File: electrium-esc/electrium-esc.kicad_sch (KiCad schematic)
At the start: 0 parts

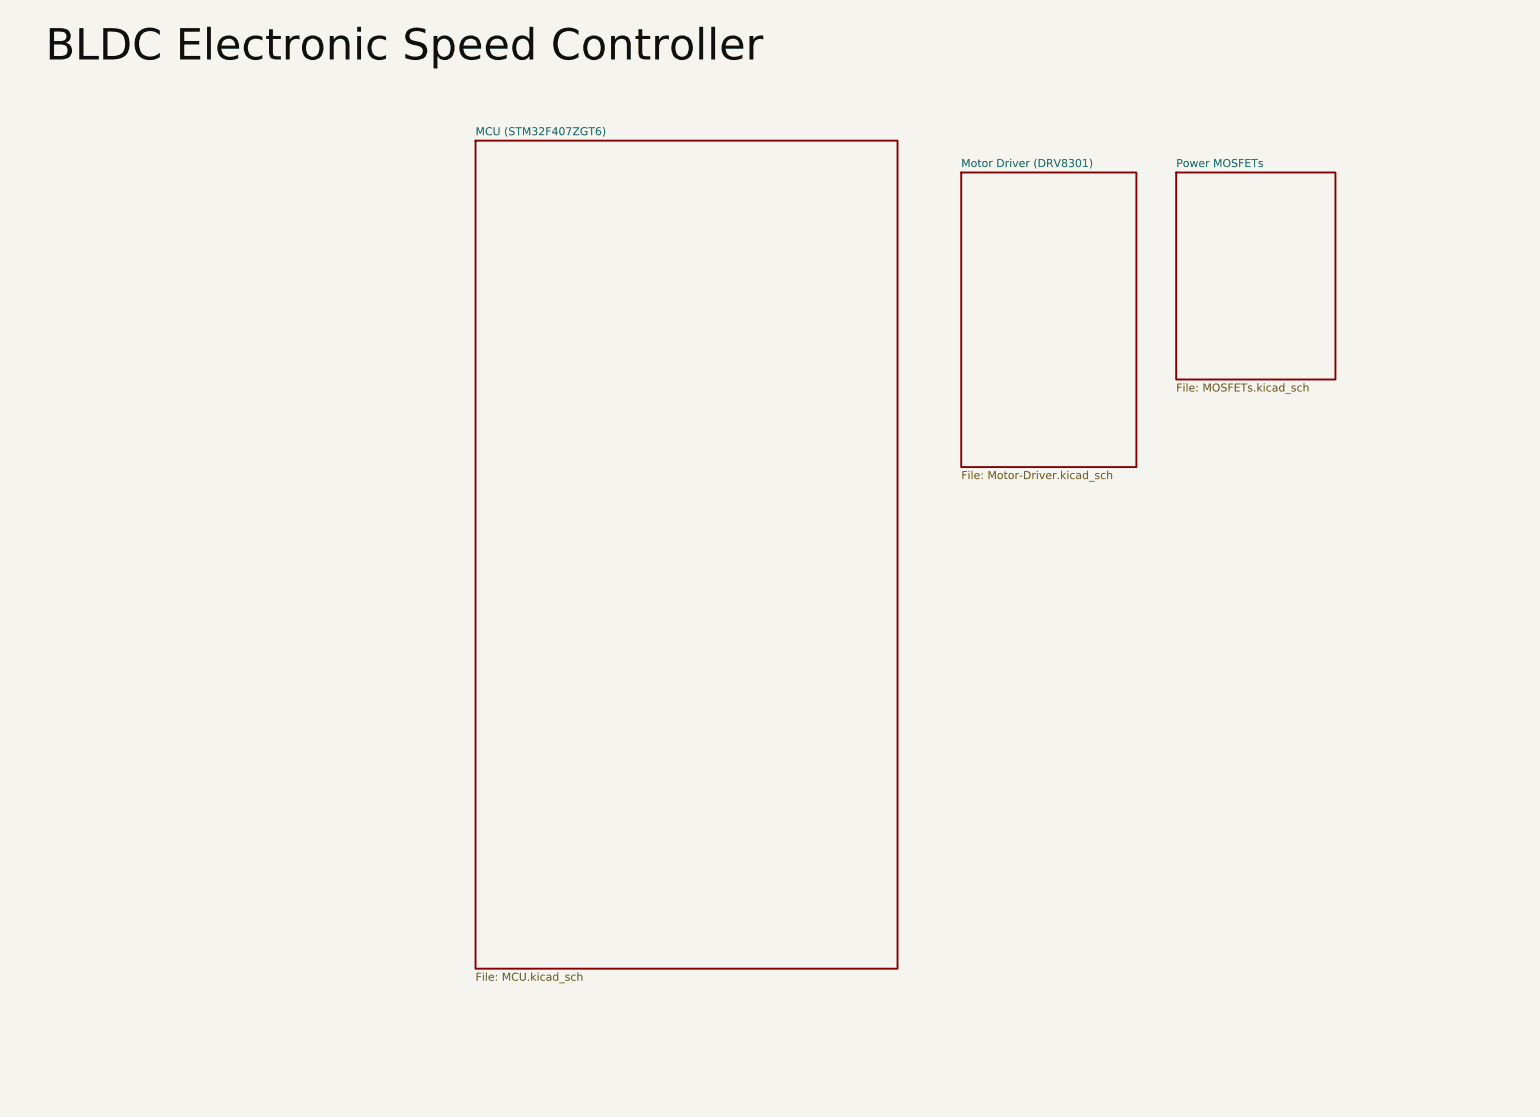
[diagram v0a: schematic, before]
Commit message: Complete Motor Driver!
Put in place passive components per documentation
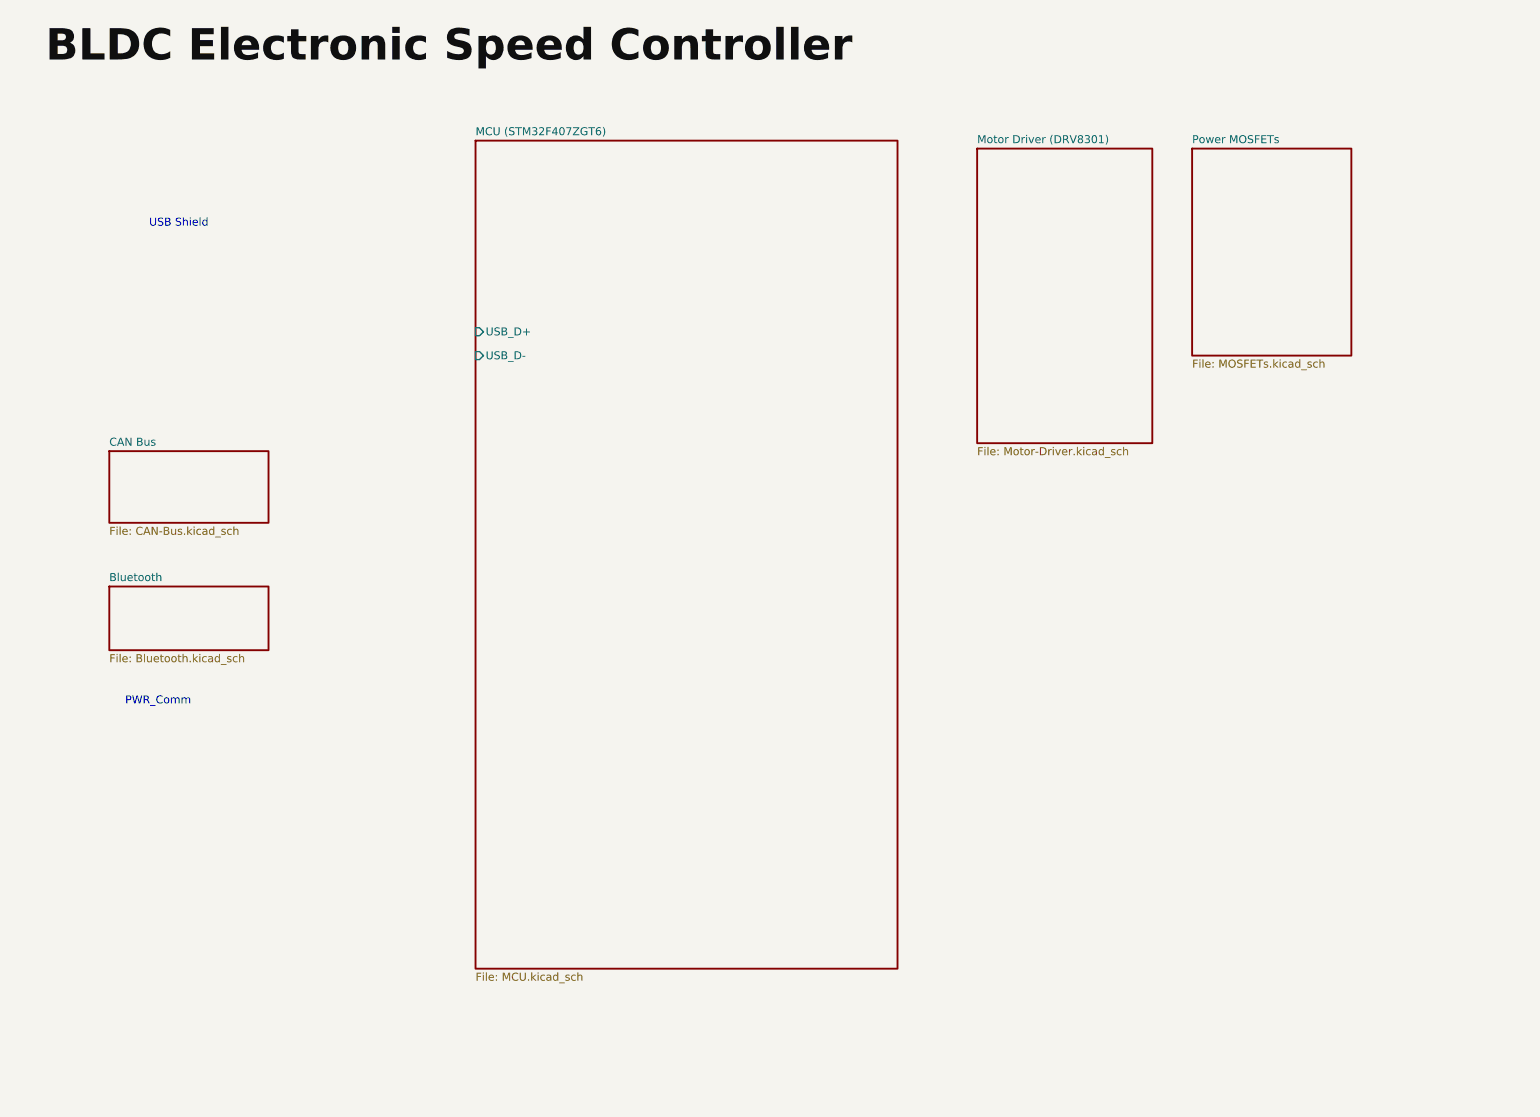
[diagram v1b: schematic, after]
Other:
- added sheet Bluetooth (Bluetooth.kicad_sch)
- added sheet CAN Bus (CAN-Bus.kicad_sch)
- sheet MCU (STM32F407ZGT6) ports: added USB_D+, USB_D-; removed none
- note added: "PWR_Comm"
- note added: "USB Shield"

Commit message: Add additional MCU connectivity
Still need to integrate NRF24L01 capabilities
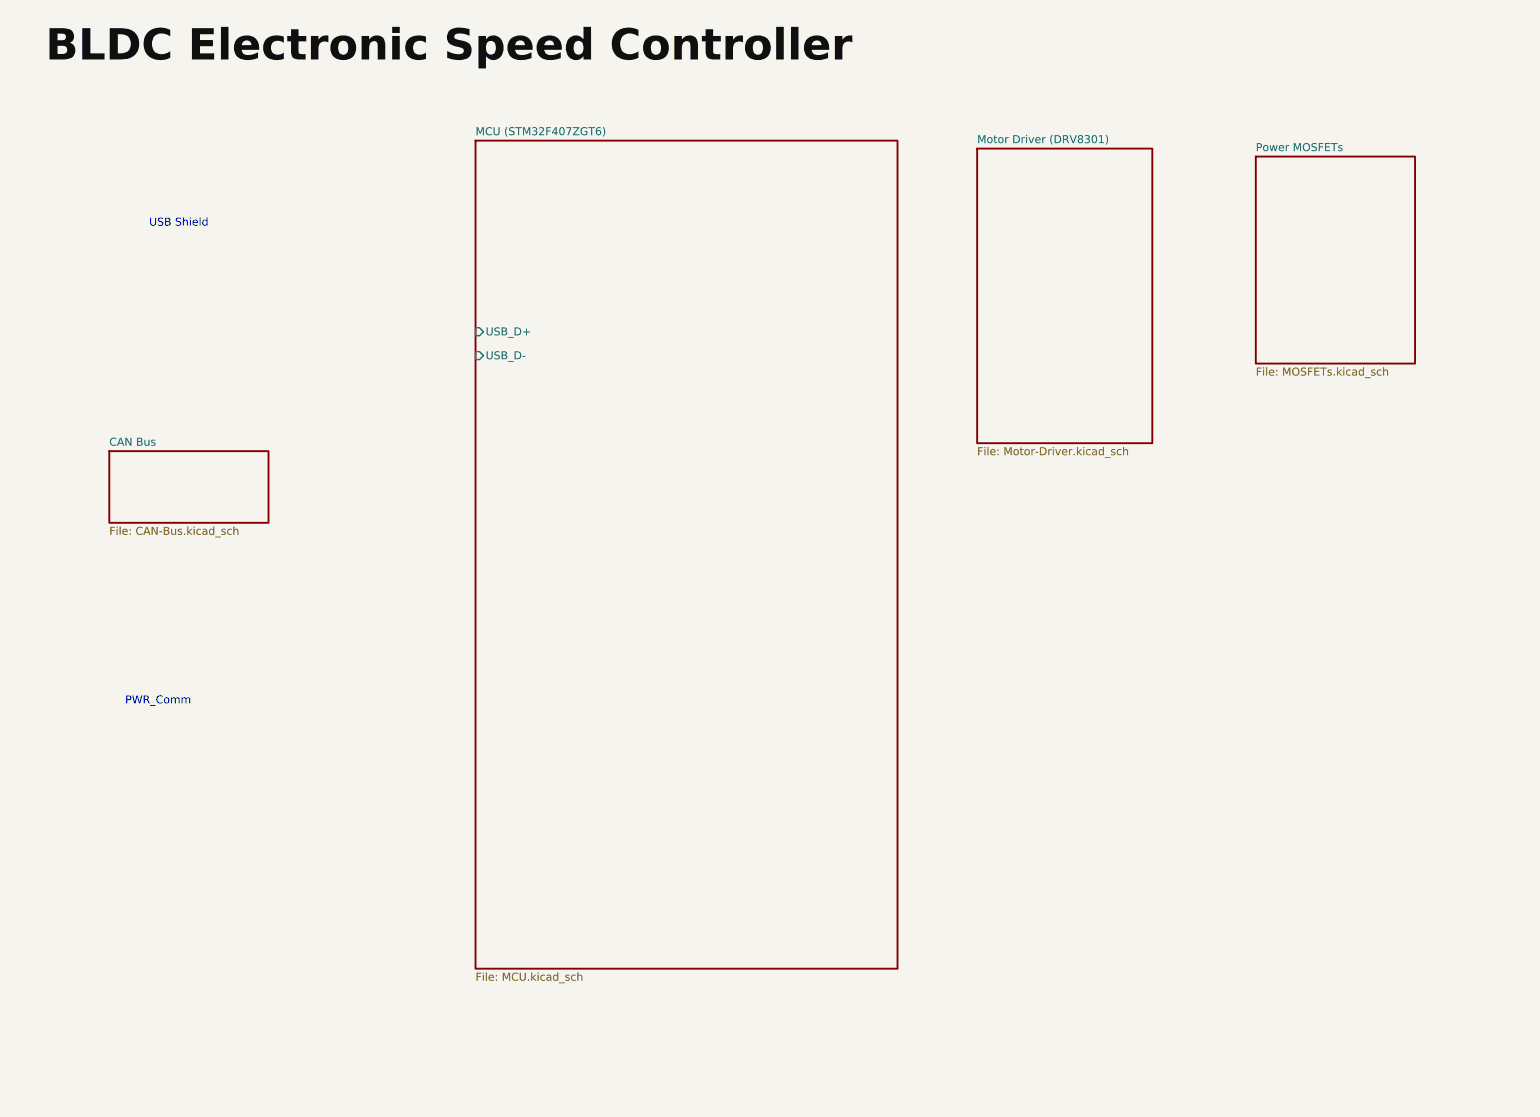
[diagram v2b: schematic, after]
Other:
- removed sheet Bluetooth
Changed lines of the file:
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@@
-    )
-  )
-  (sheet (at 29.21 109.22) (size 25.4 10.16) (fields_autoplaced)
-    (stroke (width 0.3) (type solid) (color 0 0 0 0))
-    (fill (color 0 0 0 0.0000))
-    (property "Sheet name" "Bluetooth" (id 0) (at 29.21 108.5084 0)
-      (effects (font (size 1.27 1.27)) (justify left bottom))
-    )
-    (property "Sheet file" "Bluetooth.kicad_sch" (id 1) (at 29.21 119.9646 0)
-      (effects (font (size 1.27 1.27)) (justify left top))
     )
   )
@@
     )
   )
-  (sheet (at 201.93 39.37) (size 25.4 33.02) (fields_autoplaced)
+  (sheet (at 212.09 40.64) (size 25.4 33.02) (fields_autoplaced)
     (stroke (width 0.3) (type solid) (color 0 0 0 0))
     (fill (color 0 0 0 0.0000))
-    (property "Sheet name" "Power MOSFETs" (id 0) (at 201.93 38.6584 0)
+    (property "Sheet name" "Power MOSFETs" (id 0) (at 212.09 39.9284 0)
       (effects (font (size 1.27 1.27)) (justify left bottom))
     )
-    (property "Sheet file" "MOSFETs.kicad_sch" (id 1) (at 201.93 72.9746 0)
+    (property "Sheet file" "MOSFETs.kicad_sch" (id 1) (at 212.09 74.2446 0)
       (effects (font (size 1.27 1.27)) (justify left top))
     )
@@
     (path "/9cfb263a-ea56-4cbe-86e2-b1fdf4c95ad6" (page "4"))
     (path "/f169605c-998e-4bf3-977e-b281c665fab8" (page "5"))
-    (path "/8e3fe61b-a8c8-4119-95ec-c642aa46593a" (page "6"))
   )
   (symbol_instances
@@
       (reference "#PWR?") (unit 1) (value "GND") (footprint "")
     )
+    (path "/95515899-f309-4706-b478-ef0c1d74de3d/629fd362-adcb-4532-848a-37a3527ff23a"
+      (reference "#PWR?") (unit 1) (value "+3.3V") (footprint "")
+    )
     (path "/4dcd2554-0c0c-4fca-b220-d2fb156d9cf9/63d85dea-db44-40e5-bf60-2e003de08707"
       (reference "#PWR?") (unit 1) (value "GND") (footprint "")
@@
     (path "/4dcd2554-0c0c-4fca-b220-d2fb156d9cf9/852210df-023e-4857-9fc7-2902ee6ed25c"
       (reference "#PWR?") (unit 1) (value "+3.3V") (footprint "")
+    )
+    (path "/95515899-f309-4706-b478-ef0c1d74de3d/85f66bb2-ef96-4e72-a09b-f148fef61822"
+      (reference "#PWR?") (unit 1) (value "GND") (footprint "")
     )
     (path "/4dcd2554-0c0c-4fca-b220-d2fb156d9cf9/9c4a02c0-e181-4120-84db-27bbabd088de"
@@
     )
     (path "/95515899-f309-4706-b478-ef0c1d74de3d/6e926fcb-bc57-4a6a-ac9a-7920661fd921"
-      (reference "C?") (unit 1) (value "10u") (footprint "")
+      (reference "C?") (unit 1) (value "4.7u") (footprint "")
     )
     (path "/4dcd2554-0c0c-4fca-b220-d2fb156d9cf9/72b22397-6364-471b-86f4-98c684f0c349"
@@
       (reference "C?") (unit 1) (value "100n") (footprint "")
     )
+    (path "/95515899-f309-4706-b478-ef0c1d74de3d/cdbd017b-4234-4346-8ec1-7d92071b9c8d"
+      (reference "C?") (unit 1) (value "2.2u") (footprint "")
+    )
     (path "/95515899-f309-4706-b478-ef0c1d74de3d/cdbf2009-4056-4e8b-9eca-950506bcb253"
       (reference "C?") (unit 1) (value "100n") (footprint "")
@@
       (reference "C?") (unit 1) (value "22n") (footprint "")
     )
+    (path "/95515899-f309-4706-b478-ef0c1d74de3d/d1bfab63-f8ba-4f9b-92d6-ff64e58a9173"
+      (reference "C?") (unit 1) (value "2.2u") (footprint "")
+    )
     (path "/95515899-f309-4706-b478-ef0c1d74de3d/d6d89a32-b335-48e8-aafb-d74409aee1f1"

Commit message: Add additional connections to MCU
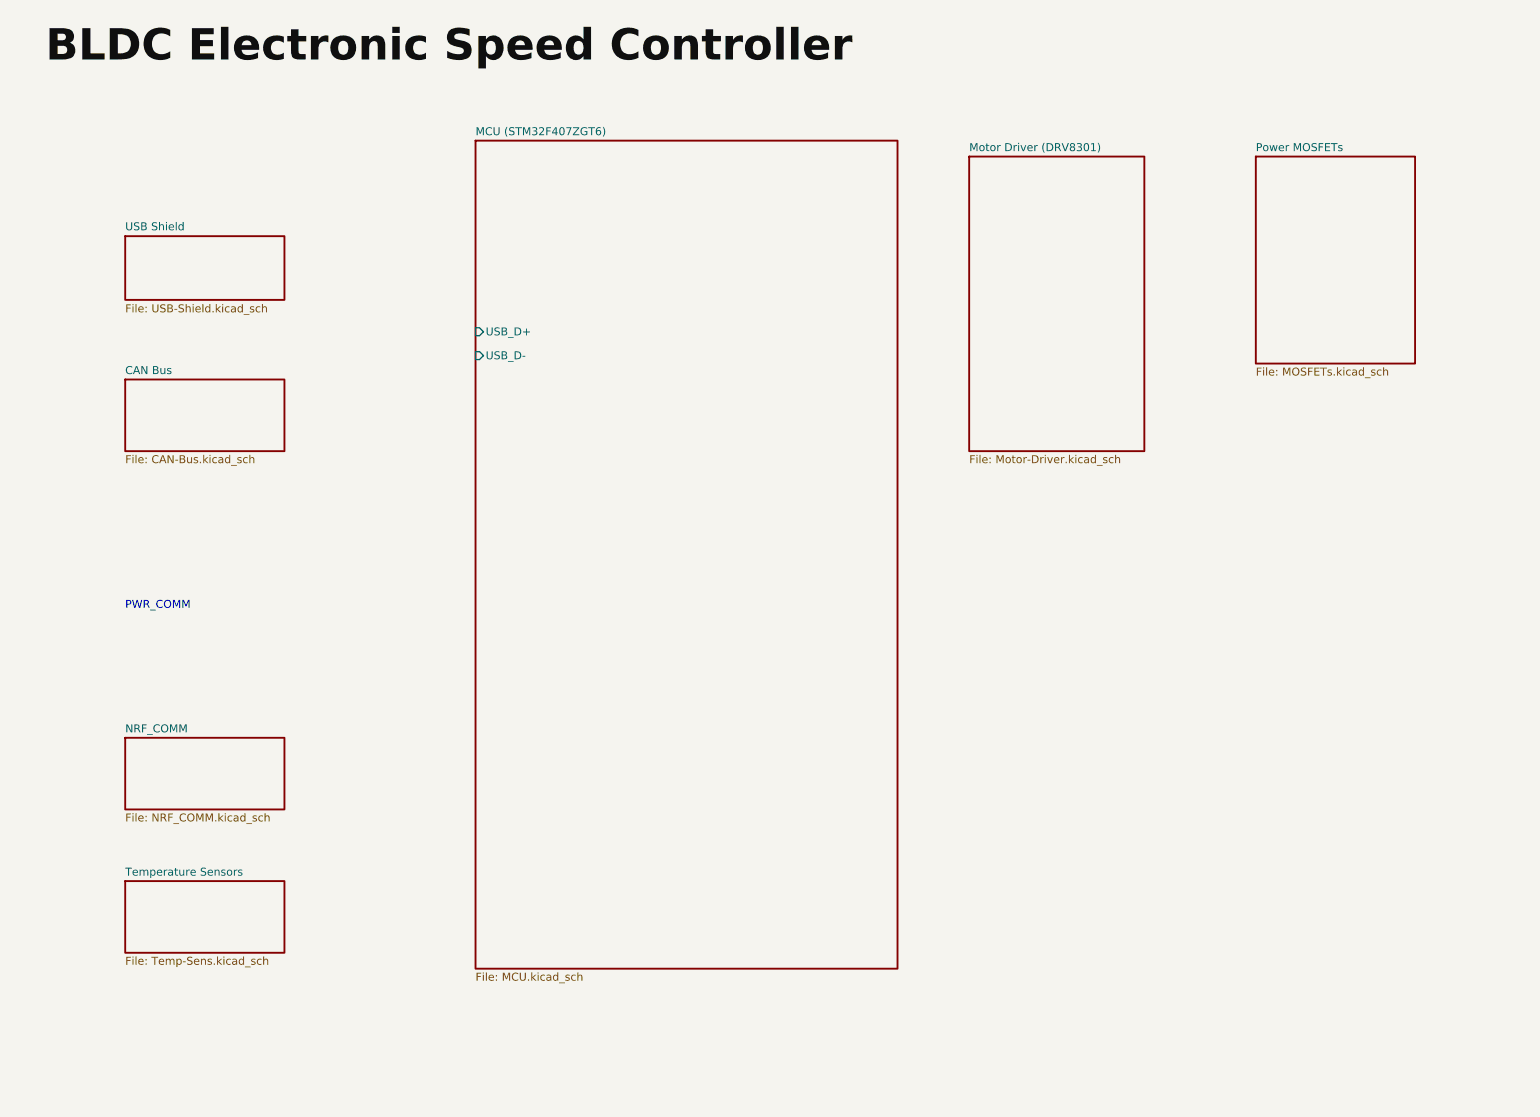
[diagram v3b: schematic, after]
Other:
- added sheet NRF_COMM (NRF_COMM.kicad_sch)
- added sheet Temperature Sensors (Temp-Sens.kicad_sch)
- added sheet USB Shield (USB-Shield.kicad_sch)
- note added: "PWR_COMM"
- note removed: "PWR_Comm"
- note removed: "USB Shield"
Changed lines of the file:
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@@
     (comment 1 "Top Level")
   )
-  (text "PWR_Comm\n" (at 31.75 128.27 0)
-    (effects (font (size 1.27 1.27)) (justify left bottom))
-  )
-  (text "USB Shield\n" (at 35.56 52.07 0)
+  (text "PWR_COMM" (at 31.75 113.03 0)
     (effects (font (size 1.27 1.27)) (justify left bottom))
   )
@@
     (effects (font (size 5 5) (thickness 1) bold) (justify left bottom))
   )
-  (sheet (at 167.64 39.37) (size 27.94 46.99) (fields_autoplaced)
+  (sheet (at 166.37 40.64) (size 27.94 46.99) (fields_autoplaced)
     (stroke (width 0.3) (type solid) (color 0 0 0 0))
     (fill (color 0 0 0 0.0000))
-    (property "Sheet name" "Motor Driver (DRV8301)" (id 0) (at 167.64 38.6584 0)
+    (property "Sheet name" "Motor Driver (DRV8301)" (id 0) (at 166.37 39.9284 0)
       (effects (font (size 1.27 1.27)) (justify left bottom))
     )
-    (property "Sheet file" "Motor-Driver.kicad_sch" (id 1) (at 167.64 86.9446 0)
+    (property "Sheet file" "Motor-Driver.kicad_sch" (id 1) (at 166.37 88.2146 0)
+      (effects (font (size 1.27 1.27)) (justify left top))
+    )
+  )
+  (sheet (at 31.75 53.34) (size 25.4 10.16) (fields_autoplaced)
+    (stroke (width 0.3) (type solid) (color 0 0 0 0))
+    (fill (color 0 0 0 0.0000))
+    (property "Sheet name" "USB Shield" (id 0) (at 31.75 52.5546 0)
+      (effects (font (size 1.27 1.27)) (justify left bottom))
+    )
+    (property "Sheet file" "USB-Shield.kicad_sch" (id 1) (at 31.75 64.1584 0)
       (effects (font (size 1.27 1.27)) (justify left top))
     )
@@
     )
   )
-  (sheet (at 29.21 87.63) (size 25.4 11.43) (fields_autoplaced)
+  (sheet (at 31.75 133.35) (size 25.4 11.43) (fields_autoplaced)
     (stroke (width 0.3) (type solid) (color 0 0 0 0))
     (fill (color 0 0 0 0.0000))
-    (property "Sheet name" "CAN Bus" (id 0) (at 29.21 86.9184 0)
+    (property "Sheet name" "NRF_COMM" (id 0) (at 31.75 132.6384 0)
       (effects (font (size 1.27 1.27)) (justify left bottom))
     )
-    (property "Sheet file" "CAN-Bus.kicad_sch" (id 1) (at 29.21 99.6446 0)
+    (property "Sheet file" "NRF_COMM.kicad_sch" (id 1) (at 31.75 145.3646 0)
+      (effects (font (size 1.27 1.27)) (justify left top))
+    )
+  )
+  (sheet (at 31.75 156.21) (size 25.4 11.43) (fields_autoplaced)
+    (stroke (width 0.3) (type solid) (color 0 0 0 0))
+    (fill (color 0 0 0 0.0000))
+    (property "Sheet name" "Temperature Sensors" (id 0) (at 31.75 155.4984 0)
+      (effects (font (size 1.27 1.27)) (justify left bottom))
+    )
+    (property "Sheet file" "Temp-Sens.kicad_sch" (id 1) (at 31.75 168.2246 0)
+      (effects (font (size 1.27 1.27)) (justify left top))
+    )
+  )
+  (sheet (at 31.75 76.2) (size 25.4 11.43) (fields_autoplaced)
+    (stroke (width 0.3) (type solid) (color 0 0 0 0))
+    (fill (color 0 0 0 0.0000))
+    (property "Sheet name" "CAN Bus" (id 0) (at 31.75 75.4884 0)
+      (effects (font (size 1.27 1.27)) (justify left bottom))
+    )
+    (property "Sheet file" "CAN-Bus.kicad_sch" (id 1) (at 31.75 88.2146 0)
       (effects (font (size 1.27 1.27)) (justify left top))
     )
@@
     (path "/9cfb263a-ea56-4cbe-86e2-b1fdf4c95ad6" (page "4"))
     (path "/f169605c-998e-4bf3-977e-b281c665fab8" (page "5"))
+    (path "/6fede19e-5ae9-46d8-9c54-8e5a277732ba" (page "6"))
+    (path "/d8de0f32-7506-49aa-9adf-28277e02e6ca" (page "7"))
+    (path "/9d2b8e53-abda-48f4-a6e0-4b62c24d8218" (page "8"))
   )
   (symbol_instances
